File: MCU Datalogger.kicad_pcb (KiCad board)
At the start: 2 copper layers, 50.8 x 30.5 mm, 29 parts, among them J1 Conn_01x04_Pin, J2 Conn_01x09_Pin, J3 Conn_01x04_Pin, J4 Conn_02x03_Odd_Even, U1 24LC1025, U2 DS1337S, U3 24LC1025, U4 ATMEGA328-AU, Y1 32.768KHz, Y2 16MHz

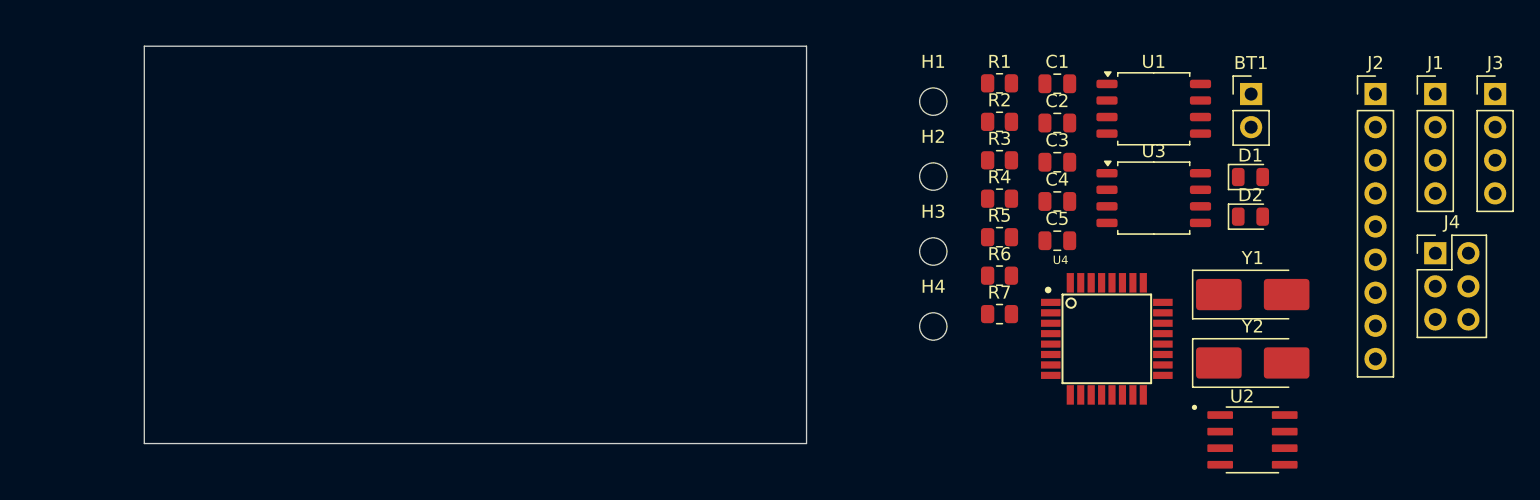
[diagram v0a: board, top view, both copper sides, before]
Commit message: placed comp
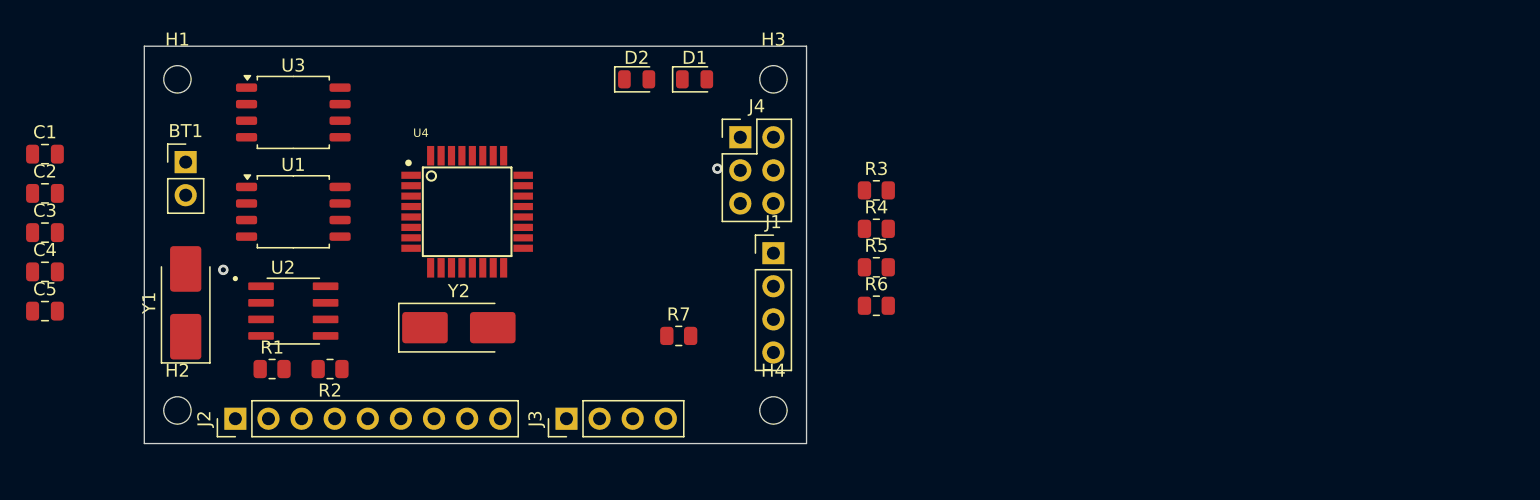
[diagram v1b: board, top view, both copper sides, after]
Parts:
- moved J2 90.9 mm to (45.1, 79.4), turned to 90 degrees
- moved BT1 81.9 mm to (41.3, 59.7)
- moved Y1 81.9 mm to (41.3, 70.5), turned to 90 degrees
- moved C1 77.8 mm to (30.5, 59.1)
- moved C2 77.8 mm to (30.5, 62.1)
- moved C3 77.8 mm to (30.5, 65.1)
- moved C4 77.8 mm to (30.5, 68.1)
- moved C5 77.8 mm to (30.5, 71.1)
- moved J3 75.5 mm to (70.5, 79.4), turned to 90 degrees
- moved U2 74.2 mm to (49.5, 71.1)
- moved U1 66.5 mm to (49.5, 63.5)
- moved U3 66.3 mm to (49.5, 55.9)
- moved Y2 61.0 mm to (62.2, 72.4)
- moved H2 60.7 mm to (40.6, 78.7)
- moved R1 60.0 mm to (47.9, 75.6)
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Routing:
- net GND: vias 0 -> 1
- net /SCK: vias 0 -> 1
